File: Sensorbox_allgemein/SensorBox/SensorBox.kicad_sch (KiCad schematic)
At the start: 26 parts, among them SW1 SW_SPST, U1 BME280, U2 PS1-O3-100, U3 Beetle ESP32-C6, U4 MC33063AD, U6 MAX31855EASA, U8 HPP845E131R5

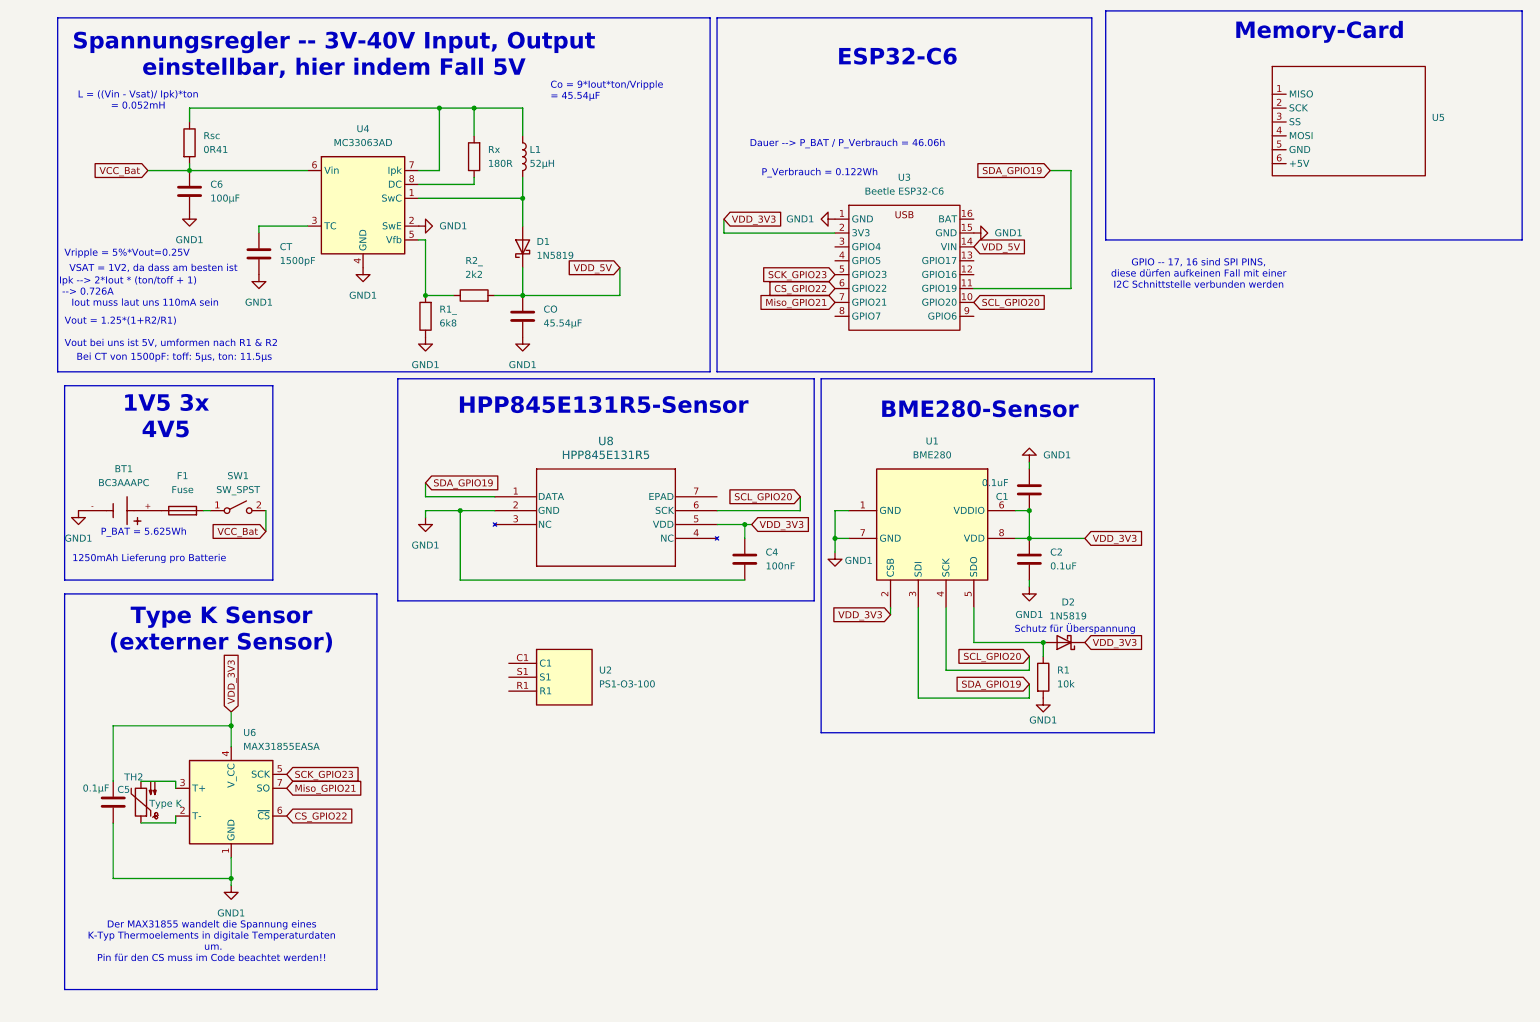
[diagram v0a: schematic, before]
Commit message: Erweiterung V3
Library für den ESP32 Wroom E erstellt, die Verbindungen ausgetauscht vom C6 zum neuen ESP und die SD Karte verbunden
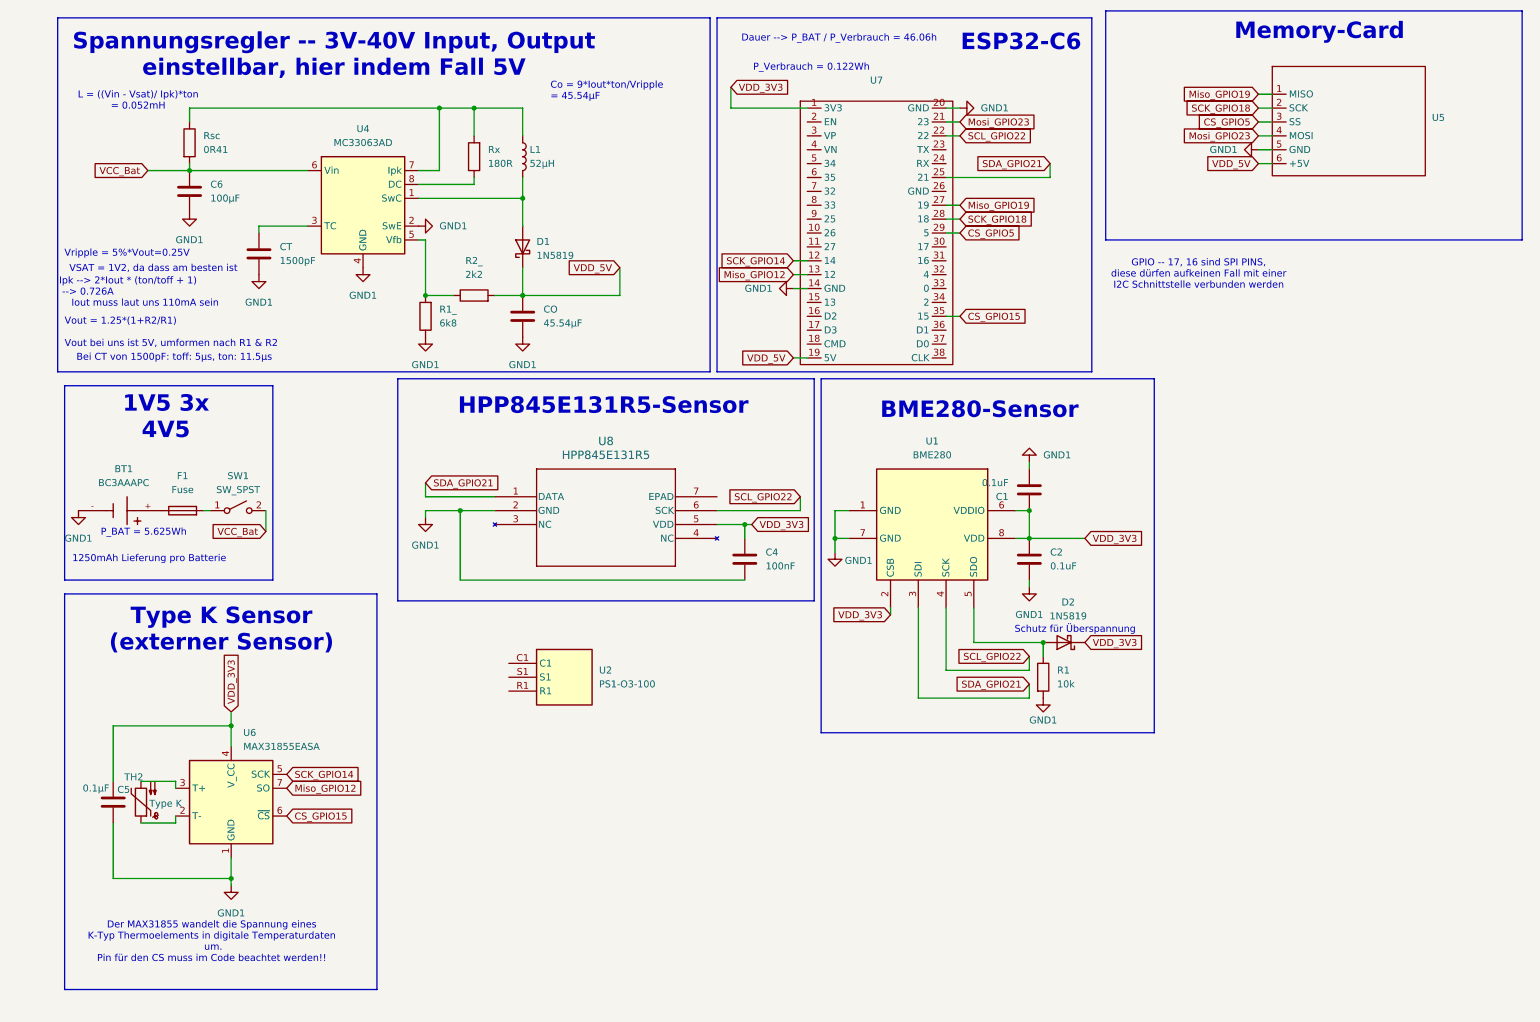
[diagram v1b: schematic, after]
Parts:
- removed U3: Beetle ESP32-C6, ESP32_C6_Firma:Beetle ESP32-C6, symbol beetle_esp32-c6:Beetle_ESP32-C6
- added U7: ~, symbol Esp32_Wroom_e:ESP32_Wroom_E32
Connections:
- net GND1: now also U5.5 (GND), U7.14 (GND), U7.20 (GND)
- net VDD_3V3: now also U7.1 (3V3)
- net VDD_5V: now also U5.6 (+5V), U7.19 (5V)
- net Miso_GPIO19: now reaches U5.1 (MISO)
- net Miso_GPIO19: now also U7.27 (19)
- net SCK_GPIO18: now reaches U5.2 (SCK)
- net SCK_GPIO18: now also U7.28 (18)
- net CS_GPIO5: now reaches U5.3 (SS)
- net CS_GPIO5: now also U7.29 (5)
- net Mosi_GPIO23: now reaches U5.4 (MOSI)
- net Mosi_GPIO23: now also U7.21 (23)
- net CS_GPIO22 renamed CS_GPIO15
- net CS_GPIO15: now also U7.35 (15)
- net Miso_GPIO21 renamed Miso_GPIO12
- net Miso_GPIO12: now also U7.13 (12)
- net SCK_GPIO23 renamed SCK_GPIO14
- net SCK_GPIO14: now also U7.12 (14)
- net SCL_GPIO20 renamed SCL_GPIO22
- net SCL_GPIO22: now also U7.22
- net SDA_GPIO19 renamed SDA_GPIO21
- net SDA_GPIO21: now also U7.25 (21)

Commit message: .
.
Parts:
- U7: footprint (none) -> ESP32_Wroom_e:ESP32_Wroom_E
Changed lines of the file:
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@@
 			)
 		)
-		(property "Footprint" ""
+		(property "Footprint" "ESP32_Wroom_e:ESP32_Wroom_E"
 			(at 151.13 31.75 0)
 			(effects

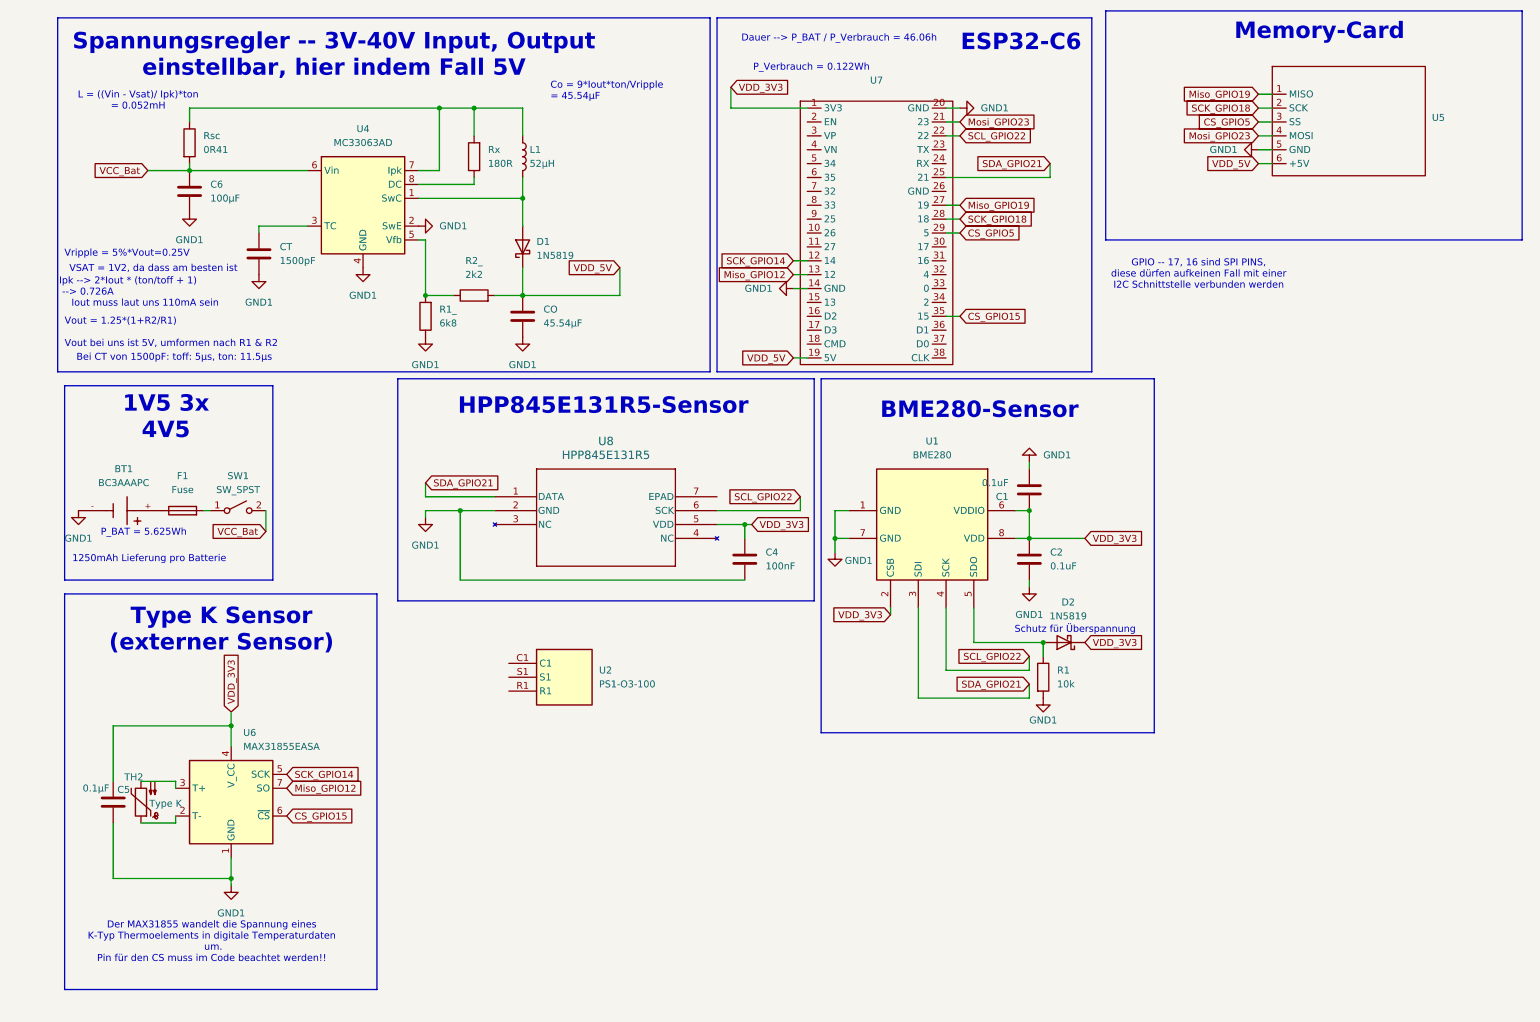
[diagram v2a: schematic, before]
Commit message: SensorboxV3
Ozonsensor eingebaut mit schaltung, Inverter Eingebaut für Ozonsensor-Schaltung
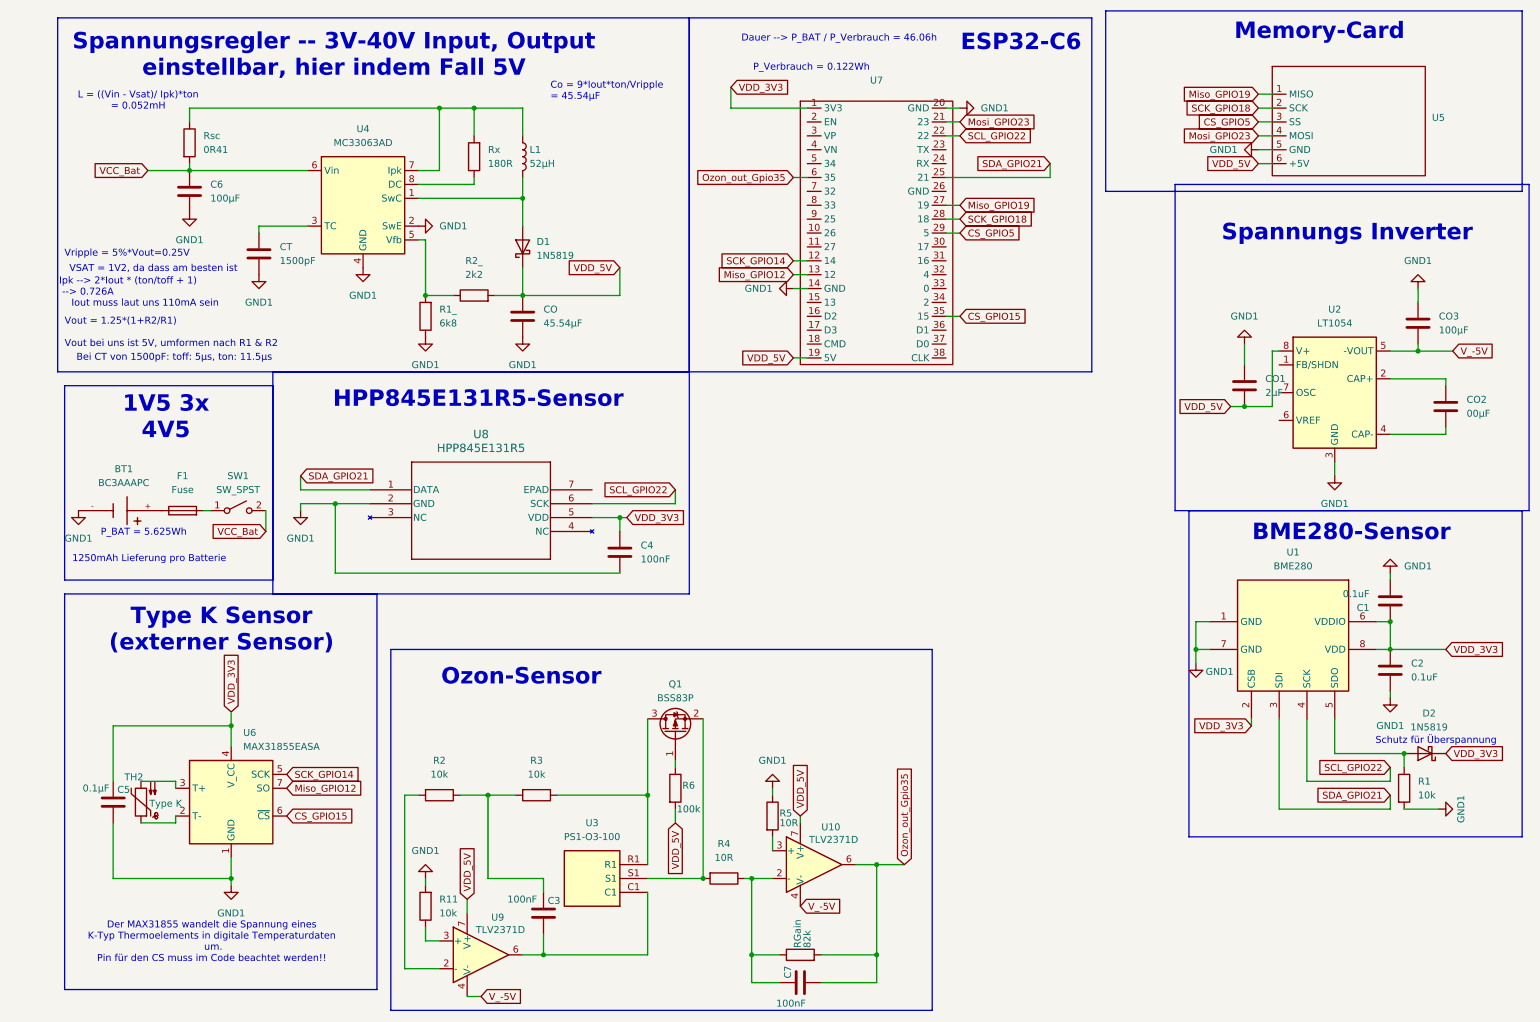
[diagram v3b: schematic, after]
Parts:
- removed U2: PS1-O3-100, PS1O3100, symbol PS1-O3-100:PS1-O3-100
- added C3, C7: 100nF, Capacitor_SMD:C_0402_1005Metric_Pad0.74x0.62mm_HandSolder, symbol Device:C
- added CO1: 2µF, Capacitor_SMD:C_0402_1005Metric_Pad0.74x0.62mm_HandSolder, symbol Device:C
- added CO2: 00µF, Capacitor_SMD:C_0402_1005Metric_Pad0.74x0.62mm_HandSolder, symbol Device:C
- added CO3: 100µF, Capacitor_SMD:C_0402_1005Metric_Pad0.74x0.62mm_HandSolder, symbol Device:C
- added Q1: BSS83P, Package_TO_SOT_SMD:SOT-23, symbol Transistor_FET:BSS83P
- added R11, R2, R3: 10k, Resistor_SMD:R_0402_1005Metric, symbol Device:R
- added R4, R5: 10R, Resistor_SMD:R_0402_1005Metric, symbol Device:R
- added R6: 100k, Resistor_SMD:R_0402_1005Metric, symbol Device:R
- added RGain: 82k, Resistor_SMD:R_0402_1005Metric, symbol Device:R
- added U10, U9: TLV2371D, Package_SO:SOIC-8_3.9x4.9mm_P1.27mm, symbol Amplifier_Operational:TLV2371D
- added U2: LT1054, symbol Regulator_SwitchedCapacitor:LT1054
- added U3: PS1-O3-100, PS1O3100, symbol PS1-O3-100:PS1-O3-100
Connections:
- net GND1: now also CO1.1, CO3.1, R11.2, R5.1, U2.3 (GND)
- net VDD_5V: now also CO1.2, R6.2, U10.7 (V+), U2.8 (V+), U9.7 (V+)
- net Ozon_out_Gpio35: now reaches U7.6 (35)
- net Ozon_out_Gpio35: now also C7.2, RGain.2, U10.6
- new net: C7.1, R4.1, RGain.1, U10.2 (-)
- new net: R5.2, U10.3 (+)
- new net: C3.1, R2.1, R3.2
- new net: C3.2, U3.C1, U9.6
- new net: Q1.2 (S), R4.2, U3.S1
- new net: CO2.1, U2.2 (CAP+)
- new net: CO2.2, U2.4 (CAP-)
- new net: Q1.3 (D), R3.1, U3.R1
- new net: R2.2, U9.2 (-)
- new net: R11.1, U9.3 (+)
- new net: Q1.1 (G), R6.1
- new net V_-5V: CO3.2, U10.4 (V-), U2.5 (-VOUT), U9.4 (V-)
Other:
- note added: "Ozon-Sensor"
- note added: "Spannungs Inverter"
- note removed: "GPIO -- 17, 16 sind SPI PINS, diese dürfen aufkeinen Fall mit einer I2C Schnittstelle verbunden werden"
- moved on the sheet: C1, C2, C4, D2, R1, U1, U8
